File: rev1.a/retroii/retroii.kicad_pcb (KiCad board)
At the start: 4 copper layers, 362 x 215.9 mm, 294 parts, among them CON1 SD_Card_SPI, J1 VGA, J10 BARREL_JACK, J11 Conn_02x10, J12 Peripheral Slot 0, J13 74LS74, J14 Game_IO_Socket, J15 Peripheral Slot 4, J16 Peripheral Slot 1, J17 Peripheral Slot 5, J18 Peripheral Slot 2, J19 Peripheral Slot 6, J2 DB9_Female_Stacked, J20 Peripheral Slot 3, J21 Peripheral Slot 7, J22 Conn_01x09, J23 Conn_01x02, J24 Headphone, J3 DB15_Female_Stacked, J6 Edge mounted connector, J7 Cassette In, J8 Cassette Out, J9 Speaker Jack, K1 PS2_KEYBOARD, K13 LM741, P1 PROP_PLUG, P2 PROP_PLUG, Q4 MPSA13, Q5 2N3904, SW1 SW_PUSH_SAFE, SW2 SPST2, SW3 SAVE, SW4 LOAD, SW5 SW_PUSH_SAFE, SW6 RESET, SW7 MISC1, SW8 MISC2, U1 74LS00, U10 74LS08, U11 LM2576-12, U12 LM2576-5, U13 LM2576-12, U14 LM2576-3.3, U15 LM2576-5, U16 Prop_P8X32A, U17 24LC256_EEPROM, U18 74LS04, U3 74LS11, U4 Prop_P8X32A, U5 24LC256_EEPROM, U6 AT28C256_EEPROM, U8 IDT7008_Dual_Port_RAM, U9 74LS32, Y1 5MHz 20pf, Y2 ECS-2100X-1MHZ, Y3 5MHz 20pf

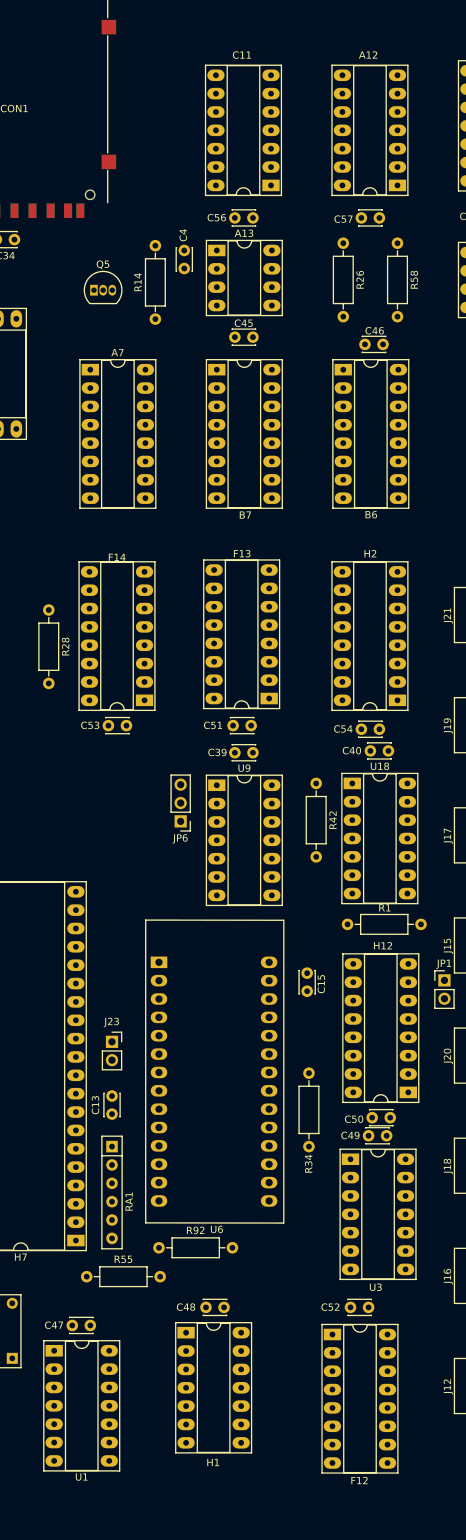
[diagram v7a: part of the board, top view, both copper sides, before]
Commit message: more layout finalization on address decoding circuit
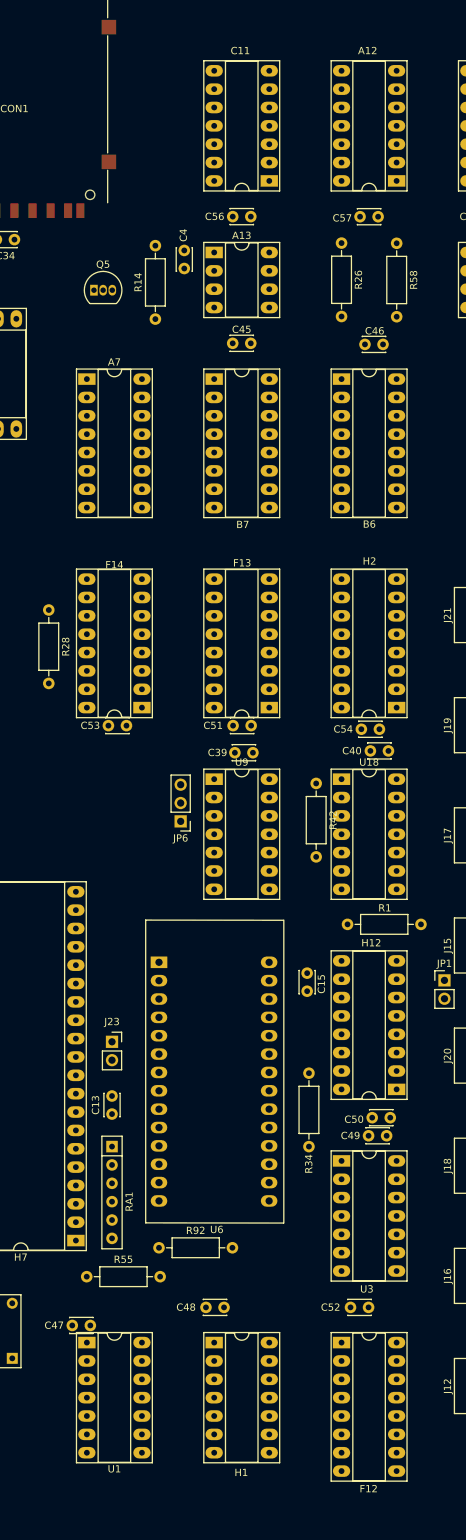
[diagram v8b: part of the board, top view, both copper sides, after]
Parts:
- moved U1 4.66 mm to (420.5, 337.1)
- moved H1 4.12 mm to (438.1, 337.1)
- moved F12 1.69 mm to (455.8, 337.1)
- moved H12 1.67 mm to (463.4, 302.1)
- moved U18 1.60 mm to (455.8, 259.2)
- moved A7 1.39 mm to (420.5, 203.8)
- moved B7 1.35 mm to (438.1, 203.8)
- moved B6 1.32 mm to (455.8, 203.8)
- moved U3 1.26 mm to (455.8, 312.0)
- moved F13 1.26 mm to (445.8, 249.3)
- moved F14 1.07 mm to (428.1, 249.3)
- moved H2 1.02 mm to (463.4, 249.3)
- moved U9 0.91 mm to (438.1, 259.2)
- moved C45 0.90 mm to (443.2, 198.8)
- moved C11 0.66 mm to (445.8, 176.4)
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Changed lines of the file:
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@@
   )
   (module Package_DIP:DIP-16_W7.62mm_Socket_LongPads (layer F.Cu)
-    (at 421 202.5)
+    (at 420.52 203.8)
     (descr "16-lead though-hole mounted DIP package, row spacing 7.62 mm (300 mils), Socket, LongPads")
     (tags "THT DIP DIL PDIP 2.54mm 7.62mm 300mil Socket LongPads")
@@
   )
   (module retroii_footprints:DIP-14_W7.62mm_Socket_LongPads (layer F.Cu)
-    (at 463.5 177 180)
+    (at 463.38 176.38 180)
     (descr "14-lead though-hole mounted DIP package, row spacing 7.62 mm (300 mils), Socket, LongPads")
     (tags "THT DIP DIL PDIP 2.54mm 7.62mm 300mil Socket LongPads")
@@
   )
   (module retroii_footprints:DIP-8_W7.62mm_Socket_LongPads (layer F.Cu)
-    (at 438.5 186)
+    (at 438.14 186.28)
     (descr "8-lead though-hole mounted DIP package, row spacing 7.62 mm (300 mils), Socket, LongPads")
     (tags "THT DIP DIL PDIP 2.54mm 7.62mm 300mil Socket LongPads")
@@
   )
   (module retroii_footprints:DIP-16_W7.62mm_Socket_LongPads (layer F.Cu)
-    (at 456 202.5)
+    (at 455.76 203.8)
     (descr "16-lead though-hole mounted DIP package, row spacing 7.62 mm (300 mils), Socket, LongPads")
     (tags "THT DIP DIL PDIP 2.54mm 7.62mm 300mil Socket LongPads")
@@
   )
   (module retroii_footprints:DIP-16_W7.62mm_Socket_LongPads (layer F.Cu)
-    (at 438.5 202.5)
+    (at 438.14 203.8)
     (descr "16-lead though-hole mounted DIP package, row spacing 7.62 mm (300 mils), Socket, LongPads")
     (tags "THT DIP DIL PDIP 2.54mm 7.62mm 300mil Socket LongPads")
@@
   )
   (module retroii_footprints:DIP-14_W7.62mm_Socket_LongPads (layer F.Cu)
-    (at 446 177 180)
+    (at 445.76 176.38 180)
     (descr "14-lead though-hole mounted DIP package, row spacing 7.62 mm (300 mils), Socket, LongPads")
     (tags "THT DIP DIL PDIP 2.54mm 7.62mm 300mil Socket LongPads")
@@
   )
   (module retroii_footprints:C_Disc_D3.0mm_W2.0mm_P2.50mm (layer F.Cu)
-    (at 443.5 198 180)
+    (at 443.2 198.85 180)
     (descr "C, Disc series, Radial, pin pitch=2.50mm, , diameter*width=3*2mm^2, Capacitor")
     (tags "C Disc series Radial pin pitch 2.50mm  diameter 3mm width 2mm Capacitor")
@@
   )
   (module retroii_footprints:C_Disc_D3.0mm_W2.0mm_P2.50mm (layer F.Cu)
-    (at 443.5 181.5 180)
+    (at 443.205 181.32 180)
     (descr "C, Disc series, Radial, pin pitch=2.50mm, , diameter*width=3*2mm^2, Capacitor")
     (tags "C Disc series Radial pin pitch 2.50mm  diameter 3mm width 2mm Capacitor")
@@
   )
   (module retroii_footprints:C_Disc_D3.0mm_W2.0mm_P2.50mm (layer F.Cu)
-    (at 461 181.5 180)
+    (at 460.82 181.33 180)
     (descr "C, Disc series, Radial, pin pitch=2.50mm, , diameter*width=3*2mm^2, Capacitor")
     (tags "C Disc series Radial pin pitch 2.50mm  diameter 3mm width 2mm Capacitor")
@@
   )
   (module retroii_footprints:DIP-16_W7.62mm_Socket_LongPads (layer F.Cu)
-    (at 454.5 336)
+    (at 455.76 337.12)
     (descr "16-lead though-hole mounted DIP package, row spacing 7.62 mm (300 mils), Socket, LongPads")
     (tags "THT DIP DIL PDIP 2.54mm 7.62mm 300mil Socket LongPads")
@@
   )
   (module retroii_footprints:DIP-16_W7.62mm_Socket_LongPads (layer F.Cu)
-    (at 445.75 248 180)
+    (at 445.76 249.26 180)
     (descr "16-lead though-hole mounted DIP package, row spacing 7.62 mm (300 mils), Socket, LongPads")
     (tags "THT DIP DIL PDIP 2.54mm 7.62mm 300mil Socket LongPads")
@@
   )
   (module retroii_footprints:DIP-16_W7.62mm_Socket_LongPads (layer F.Cu)
-    (at 428.5 248.25 180)
+    (at 428.14 249.26 180)
     (descr "16-lead though-hole mounted DIP package, row spacing 7.62 mm (300 mils), Socket, LongPads")
     (tags "THT DIP DIL PDIP 2.54mm 7.62mm 300mil Socket LongPads")
@@
   )
   (module retroii_footprints:DIP-14_W7.62mm_Socket_LongPads (layer F.Cu)
-    (at 434.25 335.75)
+    (at 438.14 337.12)
     (descr "14-lead though-hole mounted DIP package, row spacing 7.62 mm (300 mils), Socket, LongPads")
     (tags "THT DIP DIL PDIP 2.54mm 7.62mm 300mil Socket LongPads")
@@
   )
   (module retroii_footprints:DIP-16_W7.62mm_Socket_LongPads (layer F.Cu)
-    (at 463.5 248.25 180)
+    (at 463.38 249.26 180)
     (descr "16-lead though-hole mounted DIP package, row spacing 7.62 mm (300 mils), Socket, LongPads")
     (tags "THT DIP DIL PDIP 2.54mm 7.62mm 300mil Socket LongPads")
@@
   )
   (module retroii_footprints:DIP-16_W7.62mm_Socket_LongPads (layer F.Cu)
-    (at 465 302.5 180)
+    (at 463.38 302.08 180)
     (descr "16-lead though-hole mounted DIP package, row spacing 7.62 mm (300 mils), Socket, LongPads")
     (tags "THT DIP DIL PDIP 2.54mm 7.62mm 300mil Socket LongPads")
@@
   )
   (module retroii_footprints:R_Axial_DIN0207_L6.3mm_D2.5mm_P10.16mm_Horizontal (layer F.Cu)
-    (at 456 185 270)
+    (at 455.76 184.98 270)
     (descr "Resistor, Axial_DIN0207 series, Axial, Horizontal, pin pitch=10.16mm, 0.25W = 1/4W, length*diameter=6.3*2.5mm^2, http://cdn-reichelt.de/documents/datenblatt/B400/1_4W%23YAG.pdf")
     (tags "Resistor Axial_DIN0207 series Axial Horizontal pin pitch 10.16mm 0.25W = 1/4W length 6.3mm diameter 2.5mm")
@@
   )
   (module retroii_footprints:R_Axial_DIN0207_L6.3mm_D2.5mm_P10.16mm_Horizontal (layer F.Cu)
-    (at 463.5 185 270)
+    (at 463.39 185.01 270)
     (descr "Resistor, Axial_DIN0207 series, Axial, Horizontal, pin pitch=10.16mm, 0.25W = 1/4W, length*diameter=6.3*2.5mm^2, http://cdn-reichelt.de/documents/datenblatt/B400/1_4W%23YAG.pdf")
     (tags "Resistor Axial_DIN0207 series Axial Horizontal pin pitch 10.16mm 0.25W = 1/4W length 6.3mm diameter 2.5mm")
@@
   )
   (module retroii_footprints:DIP-14_W7.62mm_Socket_LongPads (layer F.Cu)
-    (at 416 338.25)
+    (at 420.52 337.12)
     (descr "14-lead though-hole mounted DIP package, row spacing 7.62 mm (300 mils), Socket, LongPads")
     (tags "THT DIP DIL PDIP 2.54mm 7.62mm 300mil Socket LongPads")
@@
   )
   (module retroii_footprints:DIP-14_W7.62mm_Socket_LongPads (layer F.Cu)
-    (at 457 311.75)
+    (at 455.76 311.98)
     (descr "14-lead though-hole mounted DIP package, row spacing 7.62 mm (300 mils), Socket, LongPads")
     (tags "THT DIP DIL PDIP 2.54mm 7.62mm 300mil Socket LongPads")
@@
   )
   (module retroii_footprints:DIP-14_W7.62mm_Socket_LongPads (layer F.Cu)
-    (at 438.5 260)
+    (at 438.14 259.16)
     (descr "14-lead though-hole mounted DIP package, row spacing 7.62 mm (300 mils), Socket, LongPads")
     (tags "THT DIP DIL PDIP 2.54mm 7.62mm 300mil Socket LongPads")
@@
   )
   (module retroii_footprints:DIP-14_W7.62mm_Socket_LongPads (layer F.Cu)
-    (at 457.25 259.75)
+    (at 455.76 259.16)
     (descr "14-lead though-hole mounted DIP package, row spacing 7.62 mm (300 mils), Socket, LongPads")
     (tags "THT DIP DIL PDIP 2.54mm 7.62mm 300mil Socket LongPads")
